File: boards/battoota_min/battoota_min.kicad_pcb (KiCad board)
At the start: 2 copper layers, 110.9 x 82.1 mm, 21 parts

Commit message: min changes
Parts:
- removed ?: , clipboard:26e710fa-e187-4e29-9de4-4e8ff64e7115
- added REF**: Tenting Puck, Alaa:Tenting_Puck, F.Cu at (253.1, 92.6)
- moved S10 3.75 mm to (264.9, 88.6)
- moved S11 3.75 mm to (264.9, 73.1)
- moved S12 3.75 mm to (281.4, 96.3)
- moved S13 3.75 mm to (281.4, 80.8)
- moved S9 3.75 mm to (264.9, 104.1)
- moved S14 2.00 mm to (271.5, 125.0)
- moved S15 2.00 mm to (288.7, 128.0)
- moved S6 2.00 mm to (245.1, 97.7)
- moved S7 2.00 mm to (243.7, 82.2)
- moved S8 2.00 mm to (242.4, 66.8)
- moved S3 1.25 mm to (227.1, 104.6)
- moved S4 1.25 mm to (224.4, 89.4)
- moved S5 1.25 mm to (221.7, 74.1)
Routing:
- net P5: track 146.8 -> 151.6 mm
- net P6: track 112.0 -> 116.3 mm
- net P4: track 93.0 -> 91.0 mm
- net P3: track 108.0 -> 106.4 mm
- net P9: track 93.5 -> 91.9 mm
- net P7: track 106.9 -> 105.6 mm
- net P8: track 90.2 -> 88.9 mm
- net P18: track 57.5 -> 58.7 mm
- net P19: track 74.5 -> 73.2 mm
- net P15: track 44.1 -> 45.4 mm
- net P16: track 71.9 -> 72.7 mm
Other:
- board size 110.9 x 82.1 mm -> 108.4 x 82.1 mm

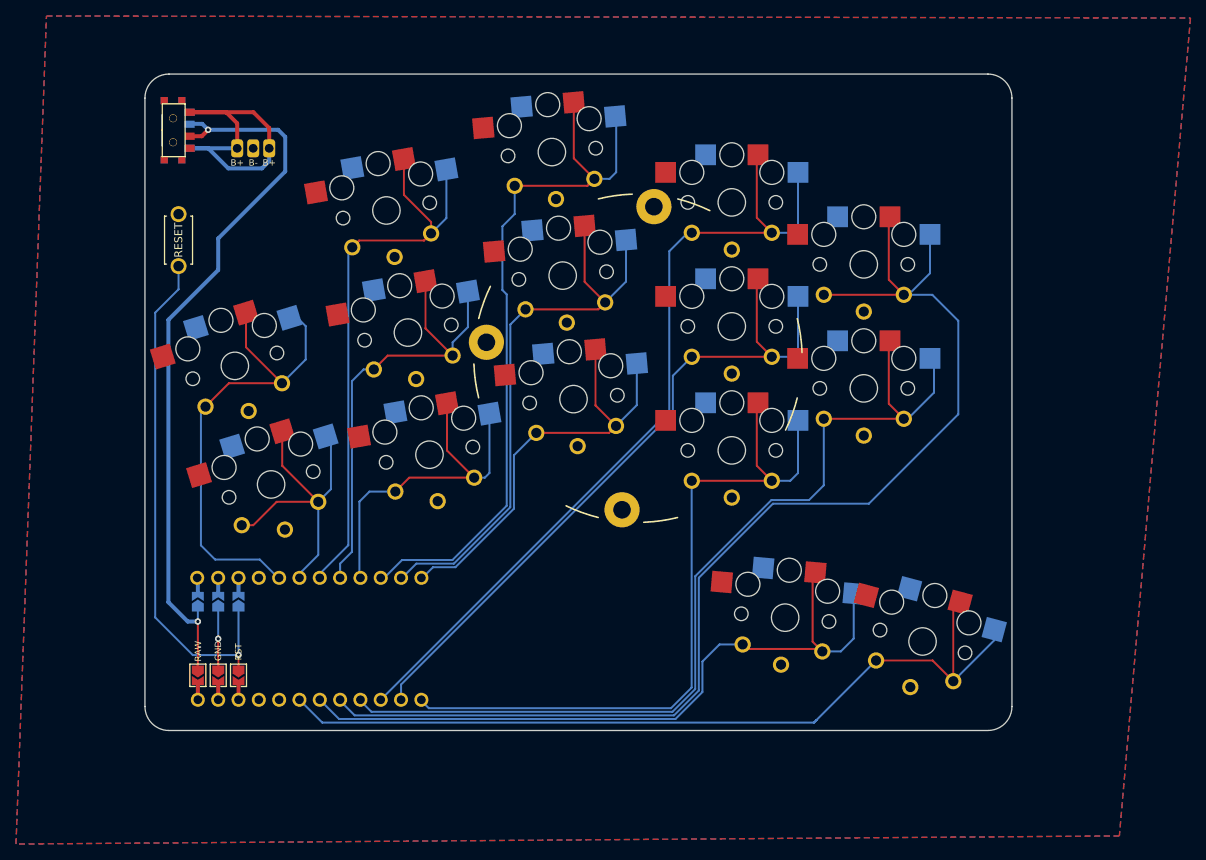
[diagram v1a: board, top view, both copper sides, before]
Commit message: new size battoota
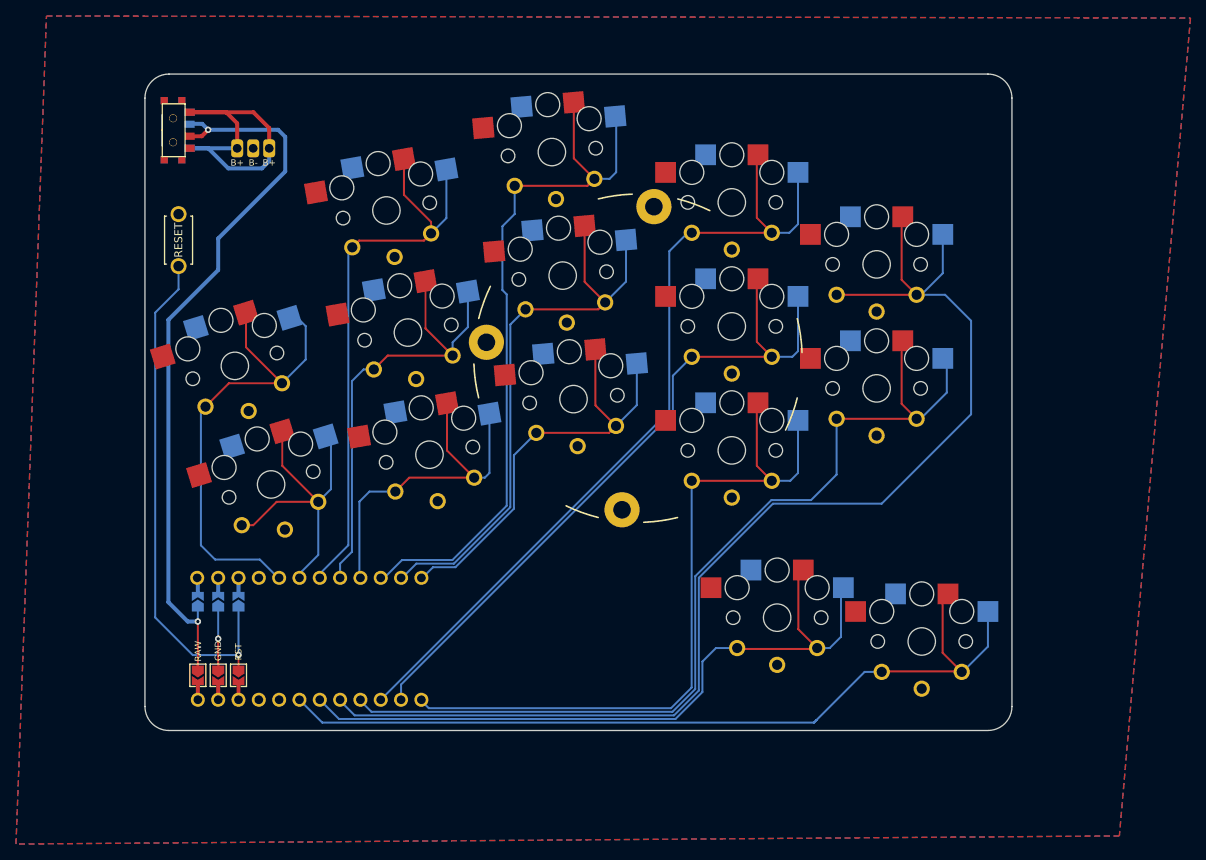
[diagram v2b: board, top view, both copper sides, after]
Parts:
- moved S12 1.60 mm to (283.0, 96.3)
- moved S13 1.60 mm to (283.0, 80.8)
- moved S14 1.00 mm to (270.5, 125.0), turned to 0 degrees
- moved S15 0.10 mm to (288.6, 128.0), turned to 0 degrees
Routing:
- net P5: track 151.6 -> 153.2 mm
- net P4: track 91.0 -> 90.0 mm
- net P6: track 116.3 -> 117.1 mm
